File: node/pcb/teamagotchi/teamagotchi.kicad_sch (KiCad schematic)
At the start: 2 parts

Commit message: first shot of the pcv
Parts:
- removed A1: Adafruit_Feather_Generic, Module:Adafruit_Feather, symbol MCU_Module:Adafruit_Feather_Generic
- removed BT1: Battery, Battery:BatteryHolder_Keystone_103_1x20mm, symbol Device:Battery
- added R1, R2, R3, R4, R5: R, Resistor_THT:R_Axial_DIN0204_L3.6mm_D1.6mm_P7.62mm_Horizontal, symbol Device:R
- added SW1, SW2, SW3, SW4, SW5: SW_Push, Button_Switch_THT:SW_SPST_Omron_B3F-40xx, symbol Switch:SW_Push
- added TFT1: ~, Library:Display-2.8, symbol dispaly:display-2.8{dblquote}
- added U1: 3406, Library:MODULE_3406, symbol 3406:3406
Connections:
- new net: R1.2, SW1.1, U1.6 (A1/0.03)
- new net: SW1.2, SW2.2, SW3.2, SW4.2, SW5.2, TFT1.50 (3/5V), U1.2 (3V3), U1.3 (3V3)
- new net: R1.1, R2.1, R3.1, R4.1, R5.1, TFT1.40 (GND), U1.4 (GND)
- new net: R4.2, SW4.1, U1.9 (A4/0.28)
- new net: TFT1.10 (D10/TFT_CS), U1.23 (P0.07)
- new net: TFT1.11 (D11/MOSI), U1.12 (MOSI)
- new net: TFT1.12 (D12/MISO), U1.13 (MISO)
- new net: TFT1.13 (D13/SCLK), U1.11 (SCK)
- new net: TFT1.8 (D8/Touch_CS), U1.24 (P0.15)
- new net: TFT1.9 (D9/TFT_DC), U1.22 (P0.11)
- new net: R3.2, SW3.1, U1.8 (A3/0.05)
- new net: R5.2, SW2.1
- new net: R2.2, SW5.1, U1.7 (A2/0.04)
- no-connect marks 0 -> 15

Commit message: first 1.0 of PCB
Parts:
- added C1: C, Capacitor_THT:C_Disc_D3.0mm_W1.6mm_P2.50mm, symbol Device:C
- added D1: 1N4001, Diode_THT:D_DO-41_SOD81_P10.16mm_Horizontal, symbol Diode:1N4001
- added M1: Motor_DC, Connector_Molex:Molex_MicroClasp_55932-0210_1x02_P2.00mm_Vertical, symbol Motor:Motor_DC
- added Q1: BC547, Package_TO_SOT_THT:TO-92_Inline, symbol Transistor_BJT:BC547
- added R6: R, Resistor_THT:R_Axial_DIN0204_L3.6mm_D1.6mm_P7.62mm_Horizontal, symbol Device:R
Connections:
- net at SW1.2, SW2.2, SW3.2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: now also C1.1, D1.1 (K), M1.1 (+)
- net at R1.1, R2.1, R3.1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: now also Q1.3 (E)
- net at TFT1.10 (D10/TFT_CS): now also U1.22 (P0.11); no longer U1.23 (P0.07)
- net at TFT1.9 (D9/TFT_DC): now also U1.23 (P0.07); no longer U1.22 (P0.11)
- net at R5.2, SW2.1: now also U1.10 (A5/0.29)
- net at U1.25 (P0.16): now also R6.1
- new net: C1.2, D1.2 (A), M1.2 (-), Q1.1 (C)
- new net: Q1.2 (B), R6.2
- no-connect marks 15 -> 14

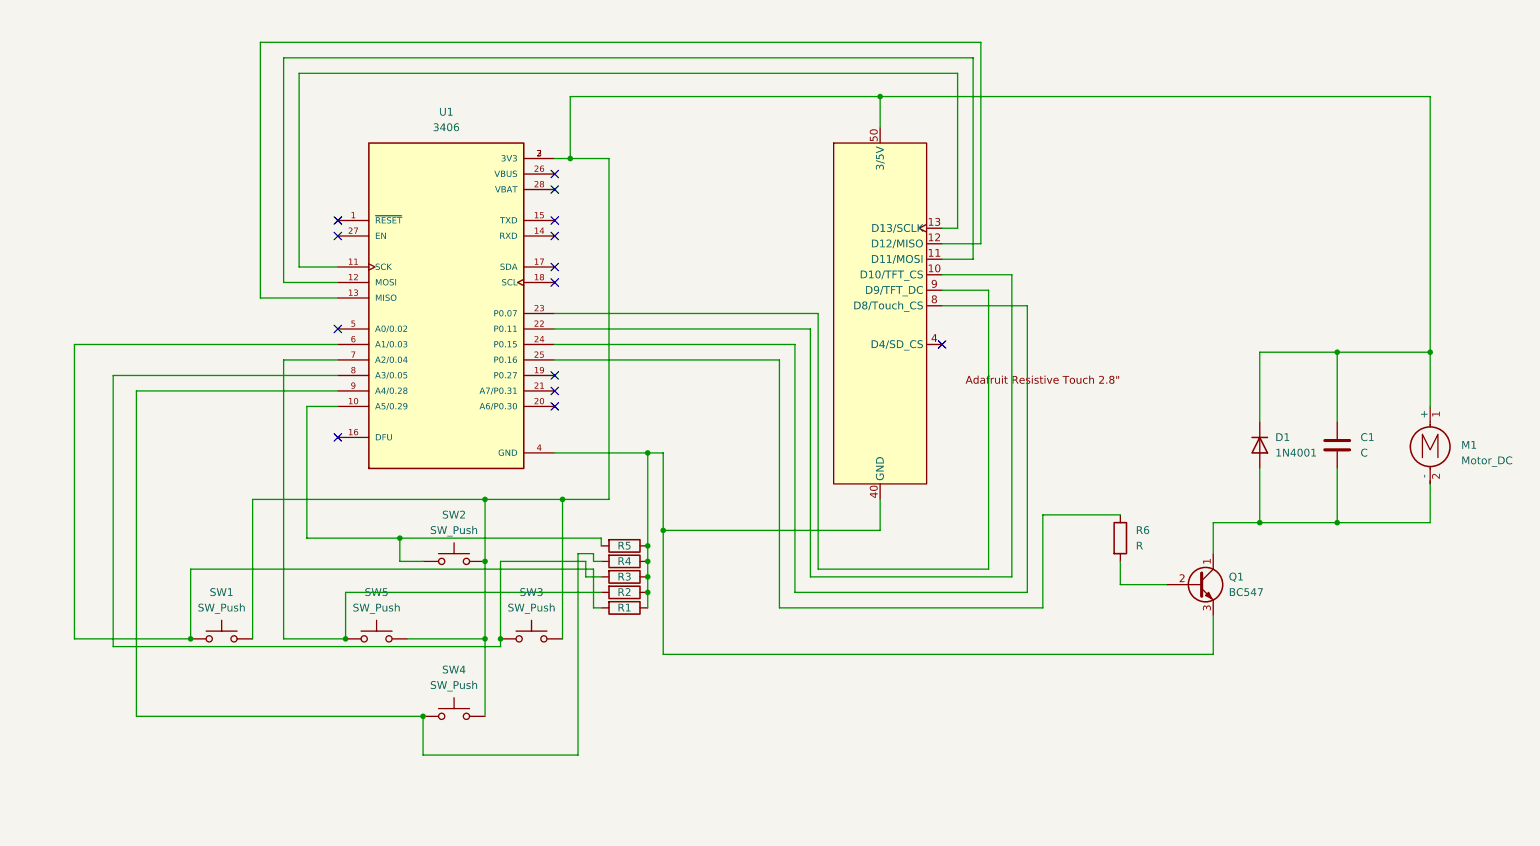
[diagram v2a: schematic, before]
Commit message: added debouncing, some beautyfications
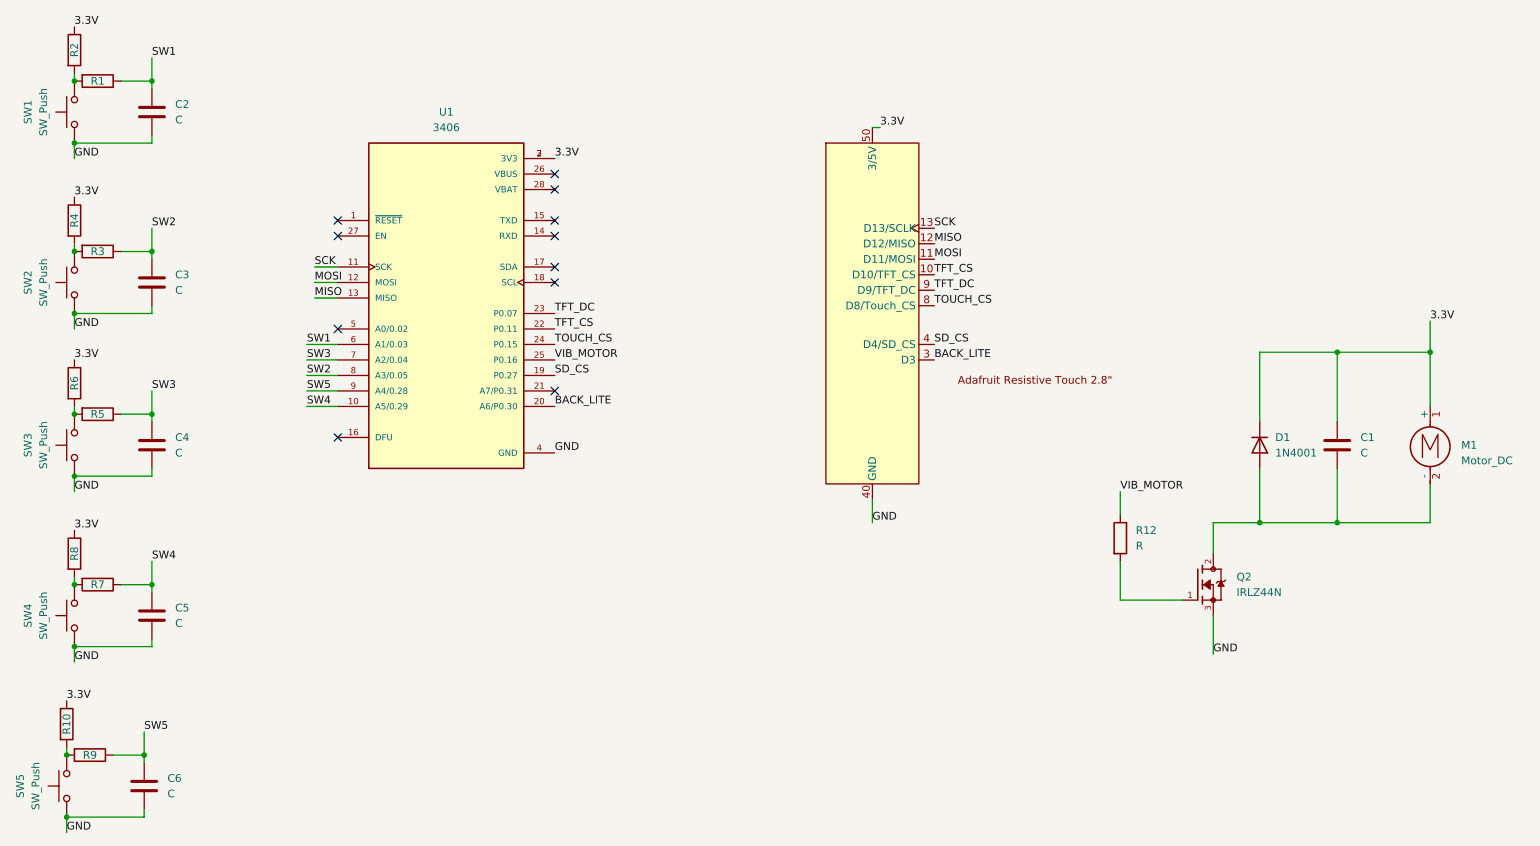
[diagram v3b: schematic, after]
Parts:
- removed Q1: BC547, Package_TO_SOT_THT:TO-92_Inline, symbol Transistor_BJT:BC547
- added C2, C3, C4, C5, C6: C, Capacitor_THT:C_Disc_D3.0mm_W1.6mm_P2.50mm, symbol Device:C
- added Q2: IRLZ44N, Library:IRLZ44N, symbol symbols:IRLZ44N
- added R10, R6, R7, R8, R9: R, Resistor_THT:R_Axial_DIN0204_L3.6mm_D1.6mm_P7.62mm_Horizontal, symbol Device:R
- renumbered R6 to R12
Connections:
- net 3.3V: now reaches C1.1, D1.1 (K), M1.1 (+), TFT1.50 (3/5V), U1.2 (3V3), U1.3 (3V3)
- net 3.3V: now also R2.1, R4.1, R10.1, R6.1, R8.1; no longer SW1.2, SW2.2, SW3.2, SW4.2, SW5.2
- net TFT_CS: now reaches TFT1.10 (D10/TFT_CS), U1.22 (P0.11)
- net MOSI: now reaches TFT1.11 (D11/MOSI), U1.12 (MOSI)
- net MISO: now reaches TFT1.12 (D12/MISO), U1.13 (MISO)
- net SCK: now reaches TFT1.13 (D13/SCLK), U1.11 (SCK)
- net SD_CS: now reaches TFT1.4 (D4/SD_CS)
- net SD_CS: now also U1.19 (P0.27)
- net TOUCH_CS: now reaches TFT1.8 (D8/Touch_CS), U1.24 (P0.15)
- net TFT_DC: now reaches TFT1.9 (D9/TFT_DC), U1.23 (P0.07)
- net at C1.2, D1.2 (A), M1.2 (-): now also Q2.2
- net at R12.2: now also Q2.1
- net BACK_LITE: now reaches U1.20 (A6/P0.30)
- net BACK_LITE: now also TFT1.3 (D3)
- net VIB_MOTOR: now reaches R12.1, U1.25 (P0.16)
- new net: R1.2, R2.2, SW1.2
- new net: R5.2, R6.2, SW3.2
- new net: R7.2, R8.2, SW4.2
- new net: R10.2, R9.2, SW5.2
- new net: R3.2, R4.2, SW2.2
- new net GND: C2.2, C3.2, C4.2, C5.2, C6.2, Q2.3, SW1.1, SW2.1, SW3.1, SW4.1, SW5.1, TFT1.40 (GND), U1.4 (GND)
- new net SW1: C2.1, R1.1, U1.6 (A1/0.03)
- new net SW2: C3.1, R3.1, U1.8 (A3/0.05)
- new net SW3: C4.1, R5.1, U1.7 (A2/0.04)
- new net SW4: C5.1, R7.1, U1.10 (A5/0.29)
- new net SW5: C6.1, R9.1, U1.9 (A4/0.28)
- no-connect marks 14 -> 11
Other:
- moved on the sheet: R1, SW1
